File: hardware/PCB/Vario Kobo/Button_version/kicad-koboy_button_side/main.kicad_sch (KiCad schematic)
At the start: 18 parts

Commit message: Restructure Vario Kobo schematic into main + power supply sheets
- Rename the KiCad project to main (main.kicad_pro/.kicad_sch/.kicad_pcb)
  and drop the empty "Alimentation" top-level sheet left by the Eagle import.
- Move the ADP160 regulator (R3, C1, C2) into a "Power supply" sub-sheet.
- Redraw the main sheet on A3 by function (barometer, Kobo connector + GPS,
  programming/MCLR, button, MAS6240 audio) with net labels instead of long
  wires, and add design notes per block.
- Add no-connect flags and PWR_FLAGs: ERC goes from 20 violations to
  11 warnings (Eagle pin types), no errors.
- Update the PCB from the schematic (renamed nets, same routing).
- README: refresh the ERC/DRC open issues and the project path.

Netlist topology, values and footprints are unchanged.

Co-Authored-By: Claude Opus 5.5 <noreply@anthropic.com>
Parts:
- added BUTTON0: SMS_J_LEAD, Vario Kobo-import-fps:SMS_J_LEAD, symbol Vario Kobo-eagle-import:SMS_J_LEAD
- added BUZZER0: PKLCS1212E2000-R1, Vario Kobo-import-fps:PKLCS1212E2000-R1-SMD, symbol Vario Kobo-eagle-import:PKLCS1212E2000-R1
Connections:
- net BUZZER_A: now also BUZZER0.P$2
- net BUZZER_B: now also BUZZER0.P$1
- net GND: now also BUTTON0.P$1 (P$2)
- net SWITCH: now also BUTTON0.P$2 (P$1)
- net SCL: now reaches MS5611.8 (SCL), PIC0.12 (*U1CTS/SCL1/CN22/RB8), R2.1
- net MCLR: now reaches C6.2, CONN_PROG0.P$4, PIC0.1 (*MCLR/VPP/RA5), R4.1
- net MAS_EN1: now reaches MAS0.P$1 (EN1), PIC0.7 (OSCI/CLKI/AN4/C1INB/C2IND/CN30/RA2)
- net MAS_EN2: now reaches MAS0.P$2 (EN2), PIC0.8 (OSCO/CLKO/AN5/C1INA/C2INC/CN29/RA3)
- net SDA: now reaches MS5611.7 (SDI/SDA), PIC0.13 (*U1RTS/SDA1/CN21/RB9), R1.1
- net PGC1: now reaches CONN_PROG0.P$2, PIC0.5 (PGC1/AN3/C1INC/C2INA/U2RX/U2BCLK/CN5/RB1)
- no-connect marks 0 -> 9
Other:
- added sheet Power supply (power.kicad_sch)
- note added: "Button: pulls SWITCH to GND, R6 10k pull-up to PROUT, read on PIC RB15."
- note added: "GPS NMEA (PA6H_TX) reaches the Kobo RX (KOBO_RX) through R5 (1k). The PIC U1TX drives KOBO_RX directly and sends the vario data between GPS bursts. PA6H_TX also goes to PIC INT1 (RB14) to detect the start of each burst. PA6H VCC comes from KOBO_EN, V_BACKUP from BATT+."
- note added: "MAS6240 piezo driver: DIN = AUDIO_OUT (PIC OC1), EN1 / EN2 from PIC RA2 / RA3. C5 / C7: charge-pump capacitors (CN1-CP1, CN2-CP2), C8 on VOUT. Buzzer between VO1 (through R7) and VO2."
- note added: "MS5611 in I2C mode (PS tied to PROUT), R1 / R2 10k I2C pull-ups. CSB (pin 4) tied to GND -> I2C address 0x77. Pin 5 is a second CSB pad, connected internally: left unconnected. SDO is unused in I2C mode."
- note added: "Power supply sheet: BATT+ (Kobo battery) -> ADP160 LDO -> PROUT. KOBO_EN (Kobo connector) enables the LDO and also supplies the PA6H GPS VCC directly."
- note added: "Programming connector (ICSP): MCLR, PGC1, PGD1 (shared with PA6H_RX), GND. No VDD pin: the board must be powered while flashing. MCLR: R4 10k pull-up + C6 100nF (PIC24F16KA102 datasheet, §2.3). The 100-470 Ω series resistor of the reference circuit is not fitted."

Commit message: Rename references and lay out a readable silkscreen
- Rename the Eagle-style references to short standard ones:
  PIC0->U1, MS5611->U2, MAS0->U3, ADP160->U4, PA6H0->U5,
  CONN_KOBO0->J1, CONN_PROG0->J2, BUTTON0->SW1, BUZZER0->BZ1.
- Move every footprint reference field next to its part, 0.8 mm text,
  clear of pads, vias and the board edge, closer to its own part than
  to any other one.
- Add footprint-owned silkscreen texts: J1/J2 pin names and a "1" next
  to pin 1 of U1-U5, so they follow the parts if they move.
- Hide value fields; drop the Eagle "1" next to the GPS and move the U1
  "*" mark to F.Fab.
- README: DRC is down from 74 to 22 warnings (footprint outlines over pads).

Co-Authored-By: Claude Opus 5.5 <noreply@anthropic.com>
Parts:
- renumbered BUZZER0 to BZ1, CONN_KOBO0 to J1, CONN_PROG0 to J2, BUTTON0 to SW1, PIC0 to U1, MS5611 to U2, MAS0 to U3, PA6H0 to U5
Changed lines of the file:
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@@
 		(in_pos_files yes)
 		(dnp no)
-		(property "Reference" "MAS0"
+		(property "Reference" "U3"
 			(at 345.44 143.51 0)
 			(show_name no)
@@
 			(project "main"
 				(path "/3589bf9b-6637-4745-bf4f-b7acb8d1884d"
-					(reference "MAS0")
-					(unit 1)
-				)
-			)
-			(project "Vario Kobo"
-				(path "/cad23409-104e-4581-9266-d814992be1c5"
-					(reference "MAS0")
+					(reference "U3")
+					(unit 1)
+				)
+			)
+			(project "Vario Kobo"
+				(path "/cad23409-104e-4581-9266-d814992be1c5"
+					(reference "U3")
 					(unit 1)
 				)
@@
 		(in_pos_files yes)
 		(dnp no)
-		(property "Reference" "CONN_PROG0"
+		(property "Reference" "J2"
 			(at 39.624 174.498 90)
 			(show_name no)
@@
 			(project "main"
 				(path "/3589bf9b-6637-4745-bf4f-b7acb8d1884d"
-					(reference "CONN_PROG0")
-					(unit 1)
-				)
-			)
-			(project "Vario Kobo"
-				(path "/cad23409-104e-4581-9266-d814992be1c5"
-					(reference "CONN_PROG0")
+					(reference "J2")
+					(unit 1)
+				)
+			)
+			(project "Vario Kobo"
+				(path "/cad23409-104e-4581-9266-d814992be1c5"
+					(reference "J2")
 					(unit 1)
 				)
@@
 		(in_pos_files yes)
 		(dnp no)
-		(property "Reference" "BUZZER0"
+		(property "Reference" "BZ1"
 			(at 345.44 191.77 0)
 			(show_name no)
@@
 			(project "main"
 				(path "/3589bf9b-6637-4745-bf4f-b7acb8d1884d"
-					(reference "BUZZER0")
-					(unit 1)
-				)
-			)
-			(project "Vario Kobo"
-				(path "/cad23409-104e-4581-9266-d814992be1c5"
-					(reference "BUZZER0")
+					(reference "BZ1")
+					(unit 1)
+				)
+			)
+			(project "Vario Kobo"
+				(path "/cad23409-104e-4581-9266-d814992be1c5"
+					(reference "BZ1")
 					(unit 1)
 				)
@@
 		(in_pos_files yes)
 		(dnp no)
-		(property "Reference" "BUTTON0"
+		(property "Reference" "SW1"
 			(at 73.66 224.79 0)
 			(show_name no)
@@
 			(project "main"
 				(path "/3589bf9b-6637-4745-bf4f-b7acb8d1884d"
-					(reference "BUTTON0")
-					(unit 1)
-				)
-			)
-			(project "Vario Kobo"
-				(path "/cad23409-104e-4581-9266-d814992be1c5"
-					(reference "BUTTON0")
+					(reference "SW1")
+					(unit 1)
+				)
+			)
+			(project "Vario Kobo"
+				(path "/cad23409-104e-4581-9266-d814992be1c5"
+					(reference "SW1")
 					(unit 1)
 				)
@@
 		(in_pos_files yes)
 		(dnp no)
-		(property "Reference" "CONN_KOBO0"
+		(property "Reference" "J1"
 			(at 36.576 50.038 90)
 			(show_name no)
@@
 			(project "main"
 				(path "/3589bf9b-6637-4745-bf4f-b7acb8d1884d"
-					(reference "CONN_KOBO0")
-					(unit 1)
-				)
-			)
-			(project "Vario Kobo"
-				(path "/cad23409-104e-4581-9266-d814992be1c5"
-					(reference "CONN_KOBO0")
+					(reference "J1")
+					(unit 1)
+				)
+			)
+			(project "Vario Kobo"
+				(path "/cad23409-104e-4581-9266-d814992be1c5"
+					(reference "J1")
 					(unit 1)
 				)
@@
 		(in_pos_files yes)
 		(dnp no)
-		(property "Reference" "PIC0"
+		(property "Reference" "U1"
 			(at 210.82 138.43 0)
 			(show_name no)
@@
 			(project "main"
 				(path "/3589bf9b-6637-4745-bf4f-b7acb8d1884d"
-					(reference "PIC0")
-					(unit 1)
-				)
-			)
-			(project "Vario Kobo"
-				(path "/cad23409-104e-4581-9266-d814992be1c5"
-					(reference "PIC0")
+					(reference "U1")
+					(unit 1)
+				)
+			)
+			(project "Vario Kobo"
+				(path "/cad23409-104e-4581-9266-d814992be1c5"
+					(reference "U1")
 					(unit 1)
 				)
@@
 		(in_pos_files yes)
 		(dnp no)
-		(property "Reference" "MS5611"
+		(property "Reference" "U2"
 			(at 212.852 70.358 0)
 			(show_name no)
@@
 			(project "main"
 				(path "/3589bf9b-6637-4745-bf4f-b7acb8d1884d"
-					(reference "MS5611")
-					(unit 1)
-				)
-			)
-			(project "Vario Kobo"
-				(path "/cad23409-104e-4581-9266-d814992be1c5"
-					(reference "MS5611")
+					(reference "U2")
+					(unit 1)
+				)
+			)
+			(project "Vario Kobo"
+				(path "/cad23409-104e-4581-9266-d814992be1c5"
+					(reference "U2")
 					(unit 1)
 				)
@@
 		(in_pos_files yes)
 		(dnp no)
-		(property "Reference" "PA6H0"
+		(property "Reference" "U5"
 			(at 60.96 113.03 0)
 			(show_name no)
@@
 			(project "main"
 				(path "/3589bf9b-6637-4745-bf4f-b7acb8d1884d"
-					(reference "PA6H0")
-					(unit 1)
-				)
-			)
-			(project "Vario Kobo"
-				(path "/cad23409-104e-4581-9266-d814992be1c5"
-					(reference "PA6H0")
+					(reference "U5")
+					(unit 1)
+				)
+			)
+			(project "Vario Kobo"
+				(path "/cad23409-104e-4581-9266-d814992be1c5"
+					(reference "U5")
 					(unit 1)
 				)
@@
 		)
 	)
+	(symbol_instances
+		(path "/3589bf9b-6637-4745-bf4f-b7acb8d1884d/bd0d3ee4-a240-4744-b530-949bc182a885"
+			(reference "U1")
+			(unit 1)
+			(value "PIC24F16KA101-X_")
+			(footprint "Vario Kobo-import-fps:SSOP20_MC")
+		)
+		(path "/3589bf9b-6637-4745-bf4f-b7acb8d1884d/c4b3c5db-8873-4f9f-8b30-bac3603923ea"
+			(reference "U2")
+			(unit 1)
+			(value "MS5607PACKAGEDNORMAL")
+			(footprint "Vario Kobo-import-fps:MS5607-02BA03")
+		)
+		(path "/3589bf9b-6637-4745-bf4f-b7acb8d1884d/18bd2956-92a3-4cd2-8bc1-59a017b26961"
+			(reference "U3")
+			(unit 1)
+			(value "MAS6240")
+			(footprint "Vario Kobo-import-fps:QFN12_3X3_LONGPADS")
+		)
+		(path "/3589bf9b-6637-4745-bf4f-b7acb8d1884d/dd785c3c-1c6a-453b-b5bb-d7f71e785dfa"
+			(reference "U5")
+			(unit 1)
+			(value "PA6H")
+			(footprint "Vario Kobo-import-fps:PA6H_PRINT")
+		)
+		(path "/3589bf9b-6637-4745-bf4f-b7acb8d1884d/8c099085-2adb-4139-be38-fbf0d478c598"
+			(reference "J1")
+			(unit 1)
+			(value "PICO-EZMATE4")
+			(footprint "Vario Kobo-import-fps:PICO-EZMATE4-PCB")
+		)
+		(path "/3589bf9b-6637-4745-bf4f-b7acb8d1884d/191aa618-6c16-4e0c-8b05-0479953e16ae"
+			(reference "J2")
+			(unit 1)
+			(value "PICO-EZMATE4")
+			(footprint "Vario Kobo-import-fps:PICO-EZMATE4-PCB")
+		)
+		(path "/3589bf9b-6637-4745-bf4f-b7acb8d1884d/7f5444fc-104c-4399-8d99-c95f48aeb974"
+			(reference "SW1")
+			(unit 1)
+			(value "SMS_J_LEAD")
+			(footprint "Vario Kobo-import-fps:SMS_J_LEAD")
+		)
+		(path "/3589bf9b-6637-4745-bf4f-b7acb8d1884d/47ae0d82-e93a-47ee-9b71-9b7f75ea2b71"
+			(reference "BZ1")
+			(unit 1)
+			(value "PKLCS1212E2000-R1")
+			(footprint "Vario Kobo-import-fps:PKLCS1212E2000-R1-SMD")
+		)
+		(path "/3589bf9b-6637-4745-bf4f-b7acb8d1884d/9b1d1e6a-e9ed-416c-b565-a066b307f2c4/50fa20a8-b821-4abd-85fc-8370d0b98102"
+			(reference "U4")
+			(unit 1)
+			(value "ADP160/161/162/163")
+			(footprint "Vario Kobo-import-fps:TSOT23-6_DDC")
+		)
+)
 	(sheet_instances
 		(path "/"

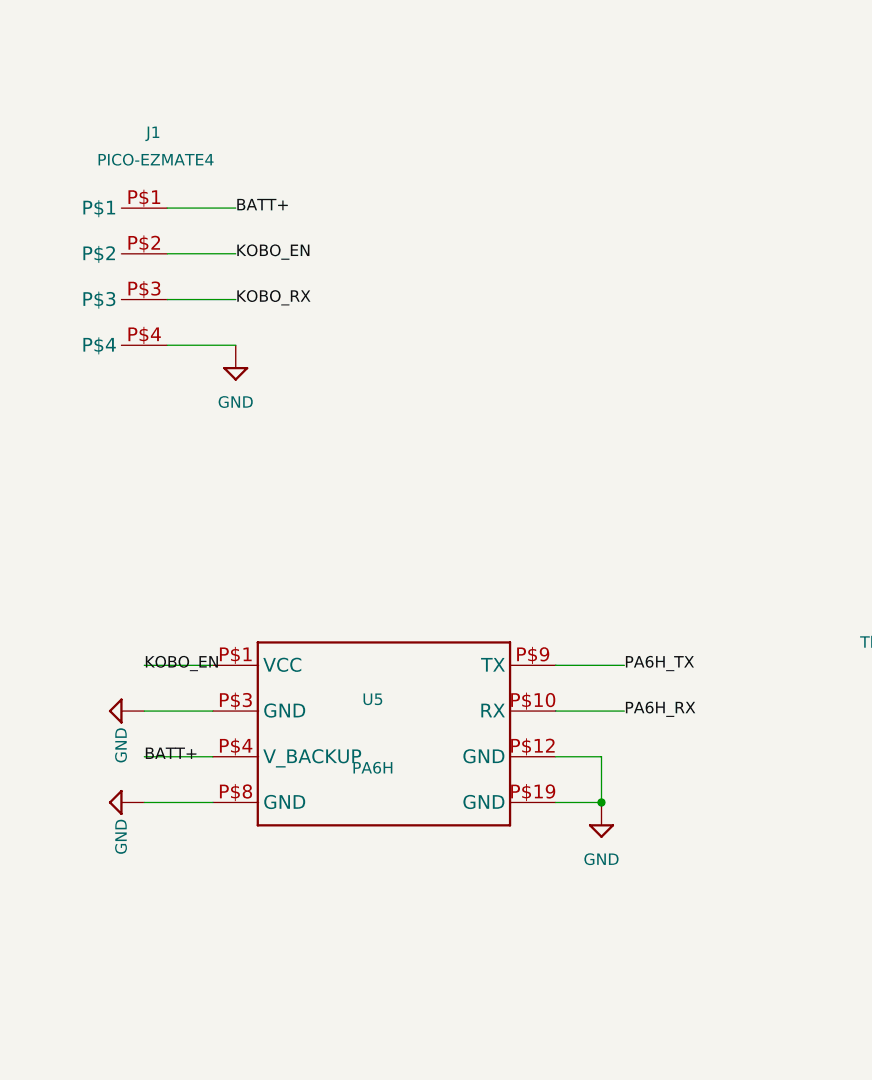
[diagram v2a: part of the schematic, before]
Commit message: Use Gekkio's FGPMMOPA6H for the GPS and clean up ERC
- U5 (GPS): replace the Eagle PA6H symbol and footprint with Gekkio's
  FGPMMOPA6H (gekkio-kicad-libs, CC BY 4.0, copied into libs/gekkio/ and
  registered in the project library tables). Same pad geometry; adds the
  datasheet's 1.2 mm NPTH under the module, a courtyard and a silkscreen
  outline clear of the pads. Unused pins flagged no-connect (datasheet:
  leave floating).
- Fix pin electrical types in the Eagle-imported symbols (connectors and
  switch passive, MAS6240/ADP160 power pins power in/out), add PWR_FLAGs
  on BATT+ and KOBO_EN, drop the now redundant one on PROUT.
- ERC: 0 errors, 0 warnings. DRC: 2 warnings (buzzer outline), no errors.
- README: refresh open issues, credit Gekkio. Ignore *.bak.

Co-Authored-By: Claude Opus 5.5 <noreply@anthropic.com>
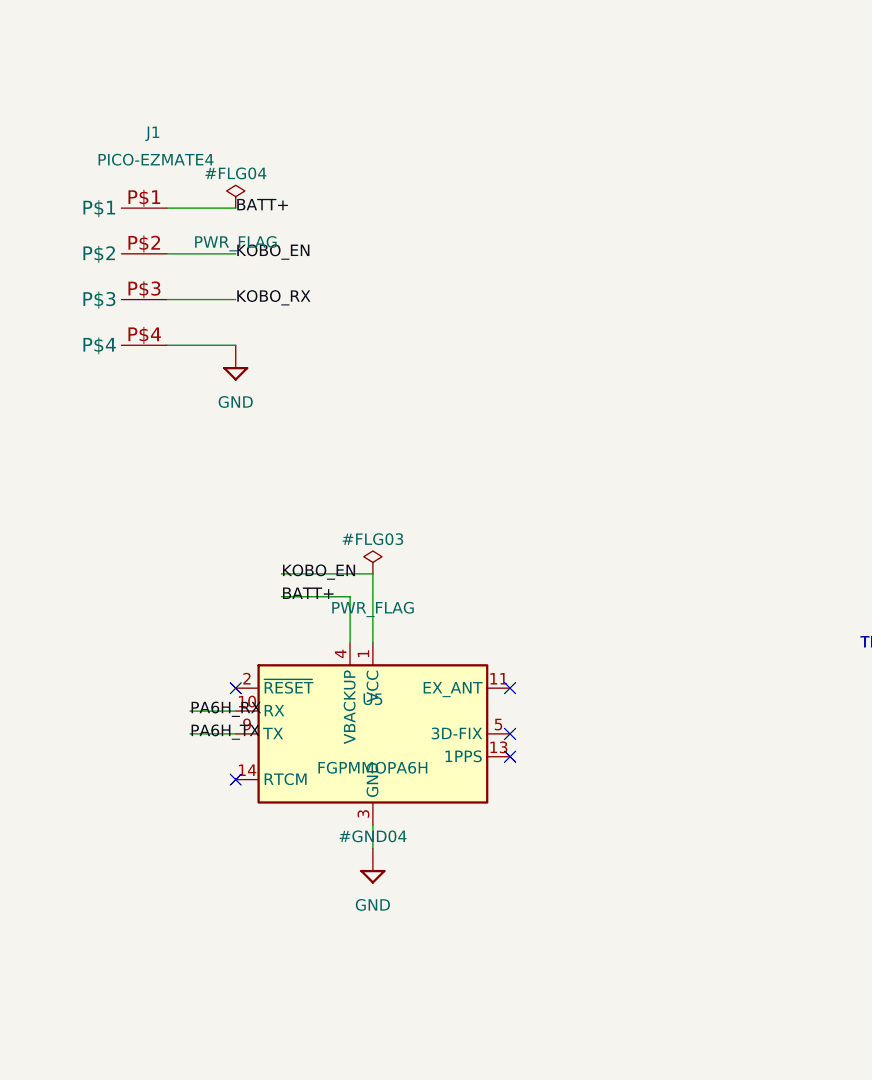
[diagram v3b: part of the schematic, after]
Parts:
- removed U5: PA6H, Vario Kobo-import-fps:PA6H_PRINT, symbol Vario Kobo-eagle-import:PA6H
- added U5: FGPMMOPA6H, Gekkio_RF_GPS:GlobalTop_FGPMMOPA6H, symbol Gekkio_RF_GPS:FGPMMOPA6H
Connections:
- net BATT+: now also U5.4 (VBACKUP)
- net GND: now also U5.12 (GND), U5.19 (GND), U5.3 (GND), U5.8 (GND)
- net KOBO_EN: now also U5.1 (VCC)
- net PA6H_RX: now also U5.10 (RX)
- net PA6H_TX: now also U5.9 (TX)
- no-connect marks 9 -> 14

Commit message: Use KiCad's standard 0603 HandSolder footprints for R and C
Replace the Eagle-imported R0603/C0603 footprints of R1-R7 and C1-C8
with Resistor_SMD:R_0603_1608Metric_Pad0.98x0.95mm_HandSolder and
Capacitor_SMD:C_0603_1608Metric_Pad1.08x0.95mm_HandSolder, easier to
solder by hand. Footprint positions and routing are unchanged; the
track ends still land inside the new pads.

Reference fields are put back at their 0.8 mm silkscreen spots and all
Value fields are hidden on F.Fab (U2's moved off F.Silkscreen too).
Netlist topology unchanged, ERC 0, DRC 0 errors / 2 warnings (BZ1 outline).

Co-Authored-By: Claude Opus 5.5 <noreply@anthropic.com>
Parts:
- C3, C4, C5, C6, C7, C8: footprint Vario Kobo-import-fps:C0603 -> Capacitor_SMD:C_0603_1608Metric_Pad1.08x0.95mm_HandSolder
- R1, R2, R4, R5, R6, R7: footprint Vario Kobo-import-fps:R0603 -> Resistor_SMD:R_0603_1608Metric_Pad0.98x0.95mm_HandSolder
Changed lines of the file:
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@@
 			)
 		)
-		(property "Footprint" "Vario Kobo-import-fps:R0603"
+		(property "Footprint" "Resistor_SMD:R_0603_1608Metric_Pad0.98x0.95mm_HandSolder"
 			(at 55.88 223.52 0)
 			(hide yes)
@@
 			)
 		)
-		(property "Footprint" "Vario Kobo-import-fps:R0603"
+		(property "Footprint" "Resistor_SMD:R_0603_1608Metric_Pad0.98x0.95mm_HandSolder"
 			(at 76.2 185.42 0)
 			(hide yes)
@@
 			)
 		)
-		(property "Footprint" "Vario Kobo-import-fps:C0603"
+		(property "Footprint" "Capacitor_SMD:C_0603_1608Metric_Pad1.08x0.95mm_HandSolder"
 			(at 317.5 152.4 0)
 			(hide yes)
@@
 			)
 		)
-		(property "Footprint" "Vario Kobo-import-fps:C0603"
+		(property "Footprint" "Capacitor_SMD:C_0603_1608Metric_Pad1.08x0.95mm_HandSolder"
 			(at 134.62 165.1 0)
 			(hide yes)
@@
 			)
 		)
-		(property "Footprint" "Vario Kobo-import-fps:R0603"
+		(property "Footprint" "Resistor_SMD:R_0603_1608Metric_Pad0.98x0.95mm_HandSolder"
 			(at 248.92 63.5 0)
 			(hide yes)
@@
 			)
 		)
-		(property "Footprint" "Vario Kobo-import-fps:C0603"
+		(property "Footprint" "Capacitor_SMD:C_0603_1608Metric_Pad1.08x0.95mm_HandSolder"
 			(at 393.7 157.48 0)
 			(hide yes)
@@
 			)
 		)
-		(property "Footprint" "Vario Kobo-import-fps:C0603"
+		(property "Footprint" "Capacitor_SMD:C_0603_1608Metric_Pad1.08x0.95mm_HandSolder"
 			(at 86.36 198.12 0)
 			(hide yes)
@@
 			)
 		)
-		(property "Footprint" "Vario Kobo-import-fps:R0603"
+		(property "Footprint" "Resistor_SMD:R_0603_1608Metric_Pad0.98x0.95mm_HandSolder"
 			(at 153.67 96.52 0)
 			(hide yes)
@@
 			)
 		)
-		(property "Footprint" "Vario Kobo-import-fps:R0603"
+		(property "Footprint" "Resistor_SMD:R_0603_1608Metric_Pad0.98x0.95mm_HandSolder"
 			(at 243.84 40.64 0)
 			(hide yes)
@@
 			)
 		)
-		(property "Footprint" "Vario Kobo-import-fps:C0603"
+		(property "Footprint" "Capacitor_SMD:C_0603_1608Metric_Pad1.08x0.95mm_HandSolder"
 			(at 180.34 58.42 0)
 			(hide yes)
@@
 			)
 		)
-		(property "Footprint" "Vario Kobo-import-fps:R0603"
+		(property "Footprint" "Resistor_SMD:R_0603_1608Metric_Pad0.98x0.95mm_HandSolder"
 			(at 386.08 144.78 0)
 			(hide yes)
@@
 			)
 		)
-		(property "Footprint" "Vario Kobo-import-fps:C0603"
+		(property "Footprint" "Capacitor_SMD:C_0603_1608Metric_Pad1.08x0.95mm_HandSolder"
 			(at 373.38 137.16 0)
 			(hide yes)
@@
 			(unit 1)
 			(value "10k")
-			(footprint "Vario Kobo-import-fps:R0603")
+			(footprint "Resistor_SMD:R_0603_1608Metric_Pad0.98x0.95mm_HandSolder")
 		)
 		(path "/3589bf9b-6637-4745-bf4f-b7acb8d1884d/c21a9cca-20fe-4619-8731-503d23ca059a"
@@
 			(unit 1)
 			(value "10k")
-			(footprint "Vario Kobo-import-fps:R0603")
+			(footprint "Resistor_SMD:R_0603_1608Metric_Pad0.98x0.95mm_HandSolder")
 		)
 		(path "/3589bf9b-6637-4745-bf4f-b7acb8d1884d/33de5bce-355c-4cd5-9eeb-48d5f4c8fe79"
@@
 			(unit 1)
 			(value "10k")
-			(footprint "Vario Kobo-import-fps:R0603")
+			(footprint "Resistor_SMD:R_0603_1608Metric_Pad0.98x0.95mm_HandSolder")
 		)
 		(path "/3589bf9b-6637-4745-bf4f-b7acb8d1884d/ad83813f-9b2a-4f43-b3db-461aae4b9187"
@@
 			(unit 1)
 			(value "1k")
-			(footprint "Vario Kobo-import-fps:R0603")
+			(footprint "Resistor_SMD:R_0603_1608Metric_Pad0.98x0.95mm_HandSolder")
 		)
 		(path "/3589bf9b-6637-4745-bf4f-b7acb8d1884d/1fe431cd-d21a-4197-ba21-947748075d43"
@@
 			(unit 1)
 			(value "10k")
-			(footprint "Vario Kobo-import-fps:R0603")
+			(footprint "Resistor_SMD:R_0603_1608Metric_Pad0.98x0.95mm_HandSolder")
 		)
 		(path "/3589bf9b-6637-4745-bf4f-b7acb8d1884d/e78e767b-ae8d-4669-a70b-b43020cc6b9e"
@@
 			(unit 1)
 			(value "1")
-			(footprint "Vario Kobo-import-fps:R0603")
+			(footprint "Resistor_SMD:R_0603_1608Metric_Pad0.98x0.95mm_HandSolder")
 		)
 		(path "/3589bf9b-6637-4745-bf4f-b7acb8d1884d/5ed4ee3f-7e30-4d33-b464-07d718f6a241"
@@
 			(unit 1)
 			(value "100nF")
-			(footprint "Vario Kobo-import-fps:C0603")
+			(footprint "Capacitor_SMD:C_0603_1608Metric_Pad1.08x0.95mm_HandSolder")
 		)
 		(path "/3589bf9b-6637-4745-bf4f-b7acb8d1884d/c6101286-389d-4628-841a-8065ab7b3c05"
@@
 			(unit 1)
 			(value "100nF")
-			(footprint "Vario Kobo-import-fps:C0603")
+			(footprint "Capacitor_SMD:C_0603_1608Metric_Pad1.08x0.95mm_HandSolder")
 		)
 		(path "/3589bf9b-6637-4745-bf4f-b7acb8d1884d/38f7514f-c295-42cf-91d6-95884bb383ae"
@@
 			(unit 1)
 			(value "100nF")
-			(footprint "Vario Kobo-import-fps:C0603")
+			(footprint "Capacitor_SMD:C_0603_1608Metric_Pad1.08x0.95mm_HandSolder")
 		)
 		(path "/3589bf9b-6637-4745-bf4f-b7acb8d1884d/99dbff2c-7f14-47e4-9267-3a017397422f"
@@
 			(unit 1)
 			(value "100nF")
-			(footprint "Vario Kobo-import-fps:C0603")
+			(footprint "Capacitor_SMD:C_0603_1608Metric_Pad1.08x0.95mm_HandSolder")
 		)
 		(path "/3589bf9b-6637-4745-bf4f-b7acb8d1884d/fdd79762-1bc6-4b4f-bf87-358730389244"
@@
 			(unit 1)
 			(value "100nF")
-			(footprint "Vario Kobo-import-fps:C0603")
+			(footprint "Capacitor_SMD:C_0603_1608Metric_Pad1.08x0.95mm_HandSolder")
 		)
 		(path "/3589bf9b-6637-4745-bf4f-b7acb8d1884d/91d760f5-3441-4741-9793-8f00704f321c"
@@
 			(unit 1)
 			(value "100nF")
-			(footprint "Vario Kobo-import-fps:C0603")
+			(footprint "Capacitor_SMD:C_0603_1608Metric_Pad1.08x0.95mm_HandSolder")
 		)
 		(path "/3589bf9b-6637-4745-bf4f-b7acb8d1884d/9b1d1e6a-e9ed-416c-b565-a066b307f2c4/ed9b2ba6-64d5-4d5c-8b48-05e57196f5dc"
@@
 			(unit 1)
 			(value "1µ")
-			(footprint "Vario Kobo-import-fps:C0603")
+			(footprint "Capacitor_SMD:C_0603_1608Metric_Pad1.08x0.95mm_HandSolder")
 		)
 		(path "/3589bf9b-6637-4745-bf4f-b7acb8d1884d/9b1d1e6a-e9ed-416c-b565-a066b307f2c4/c1f2304f-71d6-4599-b0cb-d1a3efc2a788"
@@
 			(unit 1)
 			(value "1µ")
-			(footprint "Vario Kobo-import-fps:C0603")
+			(footprint "Capacitor_SMD:C_0603_1608Metric_Pad1.08x0.95mm_HandSolder")
 		)
 		(path "/3589bf9b-6637-4745-bf4f-b7acb8d1884d/9b1d1e6a-e9ed-416c-b565-a066b307f2c4/1cf2b794-753b-4475-8f66-87fce434f05c"
@@
 			(unit 1)
 			(value "33k")
-			(footprint "Vario Kobo-import-fps:R0603")
+			(footprint "Resistor_SMD:R_0603_1608Metric_Pad0.98x0.95mm_HandSolder")
 		)
 		(path "/3589bf9b-6637-4745-bf4f-b7acb8d1884d/9b1d1e6a-e9ed-416c-b565-a066b307f2c4/50fa20a8-b821-4abd-85fc-8370d0b98102"
